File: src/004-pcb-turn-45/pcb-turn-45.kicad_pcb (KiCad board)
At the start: 2 copper layers, 20 x 20 mm, 7 parts, among them J1 CONN, J2 CONN

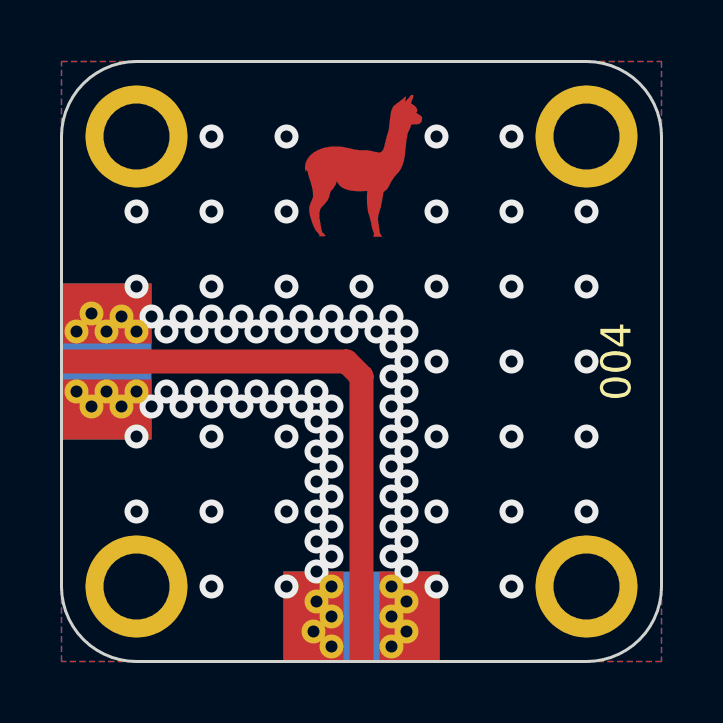
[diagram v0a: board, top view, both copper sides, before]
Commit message: changing pcb 45 turn
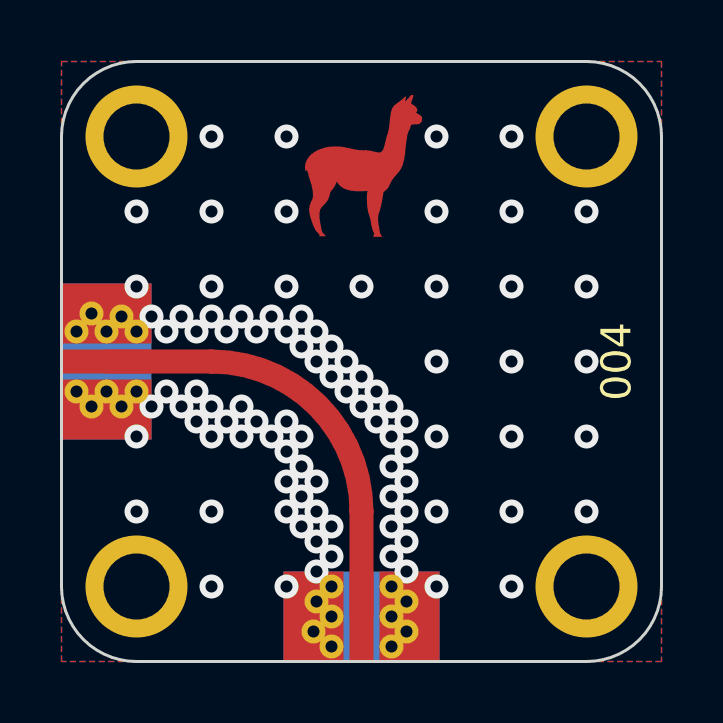
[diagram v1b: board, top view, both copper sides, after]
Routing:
- net Net-(J1-Pad1): track 16.6 -> 14.7 mm
- net GND: vias 94 -> 93
